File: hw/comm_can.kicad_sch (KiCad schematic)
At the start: 22 parts, among them IC601 ADM3055EBRIZ, J601 43650-0427, J602 43650-0427

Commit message: bugfix for wrong adc pin for batt current measurements
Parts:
- C602, C603, C608: Cost 0.0008 -> 0.0063; LCSC Part # C1525 -> CL05B104KB54PNC; Notes Rated for 16V. -> Rated for 50V.; P/N CL05B104KO5NNNC -> CL05B104KB54PNC
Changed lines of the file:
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@@
       (effects (font (size 1 1)) hide)
     )
-    (property "Datasheet" "https://datasheet.lcsc.com/lcsc/2304140030_Samsung-Electro-Mechanics-CL05B104KO5NNNC_C1525.pdf" (at 60.96 97.79 0)
+    (property "Datasheet" "https://datasheet.lcsc.com/lcsc/2304140030_Samsung-Electro-Mechanics-CL05B104KB54PNC_C307331.pdf" (at 60.96 97.79 0)
       (effects (font (size 1 1)) hide)
     )
@@
       (effects (font (size 1 1)) hide)
     )
-    (property "P/N" "CL05B104KO5NNNC" (at 60.96 97.79 0)
-      (effects (font (size 1 1)) hide)
-    )
-    (property "LCSC Part #" "C1525" (at 60.96 97.79 0)
-      (effects (font (size 1 1)) hide)
-    )
-    (property "Cost" "0.0008" (at 60.96 97.79 0)
-      (effects (font (size 1 1)) hide)
-    )
-    (property "Notes" "Rated for 16V." (at 60.96 97.79 0)
+    (property "P/N" "CL05B104KB54PNC" (at 60.96 97.79 0)
+      (effects (font (size 1 1)) hide)
+    )
+    (property "LCSC Part #" "CL05B104KB54PNC" (at 60.96 97.79 0)
+      (effects (font (size 1 1)) hide)
+    )
+    (property "Cost" "0.0063" (at 60.96 97.79 0)
+      (effects (font (size 1 1)) hide)
+    )
+    (property "Notes" "Rated for 50V." (at 60.96 97.79 0)
       (effects (font (size 1 1)) hide)
     )
@@
       (effects (font (size 1 1)) hide)
     )
-    (property "Datasheet" "https://datasheet.lcsc.com/lcsc/2304140030_Samsung-Electro-Mechanics-CL05B104KO5NNNC_C1525.pdf" (at 171.45 96.52 0)
+    (property "Datasheet" "https://datasheet.lcsc.com/lcsc/2304140030_Samsung-Electro-Mechanics-CL05B104KB54PNC_C307331.pdf" (at 171.45 96.52 0)
       (effects (font (size 1 1)) hide)
     )
@@
       (effects (font (size 1 1)) hide)
     )
-    (property "P/N" "CL05B104KO5NNNC" (at 171.45 96.52 0)
-      (effects (font (size 1 1)) hide)
-    )
-    (property "LCSC Part #" "C1525" (at 171.45 96.52 0)
-      (effects (font (size 1 1)) hide)
-    )
-    (property "Cost" "0.0008" (at 171.45 96.52 0)
-      (effects (font (size 1 1)) hide)
-    )
-    (property "Notes" "Rated for 16V." (at 171.45 96.52 0)
+    (property "P/N" "CL05B104KB54PNC" (at 171.45 96.52 0)
+      (effects (font (size 1 1)) hide)
+    )
+    (property "LCSC Part #" "CL05B104KB54PNC" (at 171.45 96.52 0)
+      (effects (font (size 1 1)) hide)
+    )
+    (property "Cost" "0.0063" (at 171.45 96.52 0)
+      (effects (font (size 1 1)) hide)
+    )
+    (property "Notes" "Rated for 50V." (at 171.45 96.52 0)
       (effects (font (size 1 1)) hide)
     )
@@
       (effects (font (size 1 1)) hide)
     )
-    (property "Datasheet" "https://datasheet.lcsc.com/lcsc/2304140030_Samsung-Electro-Mechanics-CL05B104KO5NNNC_C1525.pdf" (at 71.12 97.79 0)
+    (property "Datasheet" "https://datasheet.lcsc.com/lcsc/2304140030_Samsung-Electro-Mechanics-CL05B104KB54PNC_C307331.pdf" (at 71.12 97.79 0)
       (effects (font (size 1 1)) hide)
     )
@@
       (effects (font (size 1 1)) hide)
     )
-    (property "P/N" "CL05B104KO5NNNC" (at 71.12 97.79 0)
-      (effects (font (size 1 1)) hide)
-    )
-    (property "LCSC Part #" "C1525" (at 71.12 97.79 0)
-      (effects (font (size 1 1)) hide)
-    )
-    (property "Cost" "0.0008" (at 71.12 97.79 0)
-      (effects (font (size 1 1)) hide)
-    )
-    (property "Notes" "Rated for 16V." (at 71.12 97.79 0)
+    (property "P/N" "CL05B104KB54PNC" (at 71.12 97.79 0)
+      (effects (font (size 1 1)) hide)
+    )
+    (property "LCSC Part #" "CL05B104KB54PNC" (at 71.12 97.79 0)
+      (effects (font (size 1 1)) hide)
+    )
+    (property "Cost" "0.0063" (at 71.12 97.79 0)
+      (effects (font (size 1 1)) hide)
+    )
+    (property "Notes" "Rated for 50V." (at 71.12 97.79 0)
       (effects (font (size 1 1)) hide)
     )
@@
       (effects (font (size 1 1)) hide)
     )
-    (property "Datasheet" "~" (at 189.23 99.06 0)
-      (effects (font (size 1 1)) hide)
-    )
+    (property "Datasheet" "" (at 189.23 99.06 0)
+      (effects (font (size 1 1)) hide)
+    )

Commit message: init sch changes
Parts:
- removed C601, C606: 10uF, Capacitor_SMD:C_0402_1005Metric, symbol Device:C_Small
- removed C602, C603, C608: 100nF, Capacitor_SMD:C_0402_1005Metric, symbol Device:C_Small
- removed C604, C607: 10nF, Capacitor_SMD:C_0402_1005Metric, symbol Device:C_Small
- removed C605: 220nF, Capacitor_SMD:C_0402_1005Metric, symbol Device:C_Small
- removed D601: CDSOT23-T24CAN, footprints:bourns_CDSOT23_T24CAN, symbol bourns_CDSOT23_T24CAN:CDSOT23-T24CAN
- removed IC601: ADM3055EBRIZ, footprints:analog_ADM3055EBRIZ, symbol analog_ADM3055EBRIZ:ADM3055EBRIZ
- removed J601, J602: 43650-0427, footprints:molex_microfit_43650_0427, symbol molex_microfit_43650_0427:43650-0427
- removed JP601: Termination Resistors, Connector_PinHeader_2.54mm:PinHeader_1x02_P2.54mm_Vertical, symbol Jumper:Jumper_2_Open
- removed L601, L602: 1.8k, Inductor_SMD:L_0402_1005Metric, symbol Device:FerriteBead_Small
- removed R601: 0, Resistor_SMD:R_0402_1005Metric, symbol Device:R
- removed R602, R603: 60.4, Resistor_SMD:R_0402_1005Metric, symbol Device:R
- removed TP601: CAN RX TP, TestPoint:TestPoint_Pad_1.0x1.0mm, symbol Connector:TestPoint
- removed TP602: CAN TX TP, TestPoint:TestPoint_Pad_1.0x1.0mm, symbol Connector:TestPoint
- removed TP603: CAN L TP, TestPoint:TestPoint_Pad_1.0x1.0mm, symbol Connector:TestPoint
- removed TP604: CAN H TP, TestPoint:TestPoint_Pad_1.0x1.0mm, symbol Connector:TestPoint
- added C24, C25: 100nF, symbol Device:C_Small
- added D5: CDSOT23-T24CAN, footprints:bourns_CDSOT23_T24CAN, symbol bourns_CDSOT23_T24CAN:CDSOT23-T24CAN
- added J2, J3: 43650-0427, footprints:molex_microfit_43650_0427, symbol molex_microfit_43650_0427:43650-0427
- added JP1: Termination Resistors, Connector_PinHeader_2.54mm:PinHeader_1x02_P2.54mm_Vertical, symbol Jumper:Jumper_2_Open
- added R12: 120, symbol Device:R_Small
- added TP10: CAN_{TX}, symbol Connector:TestPoint
- added TP11: CAN_{VCC}, symbol Connector:TestPoint
- added TP12: CAN_{H}, symbol Connector:TestPoint
- added TP13: CAN_{L}, symbol Connector:TestPoint
- added TP14: CAN_{GND}, symbol Connector:TestPoint
- added TP9: CAN_{RX}, symbol Connector:TestPoint
- added U7: ISO1044BD, Package_SO:SOIC-8_3.9x4.9mm_P1.27mm, symbol Interface_CAN_LIN:ISO1044BD
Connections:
- net +3V3: now also C24.1, U7.1 (VCC1)
- net CAN_RX: now also TP9.1, U7.3 (RXD)
- net CAN_TX: now also TP10.1, U7.2 (TXD)
- net GND: now also C24.2, U7.4 (GND1)
- new net: JP1.2 (B), R12.1
- new net CAN_{GND}: C25.2, D5.3 (K3), J2.2, J3.2, TP14.1, U7.7 (GND2)
- new net CAN_{H}: D5.1 (K1), J2.3, J3.3, R12.2, TP12.1, U7.6 (CANH)
- new net CAN_{L}: D5.2 (K2), J2.4, J3.4, JP1.1 (A), TP13.1, U7.5 (CANL)
- new net CAN_{VCC}: C25.1, J2.1, J3.1, TP11.1, U7.8 (VCC2)
- no-connect marks 4 -> 0
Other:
- note removed: "Must be close to V_ISO_In"
- note removed: "Must be close to V_ISO_Out"

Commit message: v0.3.0rc (v1.0.0rc) sch complete
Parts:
- removed C24: 100nF, symbol Device:C_Small
- removed J3: 43650-0427, footprints:molex_microfit_43650_0427, symbol molex_microfit_43650_0427:43650-0427
- removed TP10: CAN_{TX}, symbol Connector:TestPoint
- removed TP11: CAN_{VCC}, symbol Connector:TestPoint
- removed TP12: CAN_{H}, symbol Connector:TestPoint
- removed TP13: CAN_{L}, symbol Connector:TestPoint
- removed TP14: CAN_{GND}, symbol Connector:TestPoint
- removed TP9: CAN_{RX}, symbol Connector:TestPoint
- added C601: 4.7u, Resistor_SMD:R_0402_1005Metric, symbol Device:C_Small
- added C603: 100n, Resistor_SMD:R_0402_1005Metric, symbol Device:C_Small
- added C604, C605: 1u, Resistor_SMD:R_0402_1005Metric, symbol Device:C_Small
- added D601, D602: GRN, LED_SMD:LED_0402_1005Metric, symbol Device:LED_Small
- added J602: CAN Header, footprints:molex_microfit_43650_0427, symbol molex_microfit_43650_0427:43650-0427
- added R601: 330, Resistor_SMD:R_0402_1005Metric, symbol Device:R_Small
- added R603: 1k, Resistor_SMD:R_0402_1005Metric, symbol Device:R_Small
- added SB601, SB602: Jumper, Jumper:SolderJumper-2_P1.3mm_Open_TrianglePad1.0x1.5mm, symbol Jumper:SolderJumper_2_Bridged
- added TP601: VBUS_CAN, TestPoint:TestPoint_Keystone_5000-5004_Miniature, symbol Connector:TestPoint
- added TP602: GND, TestPoint:TestPoint_Keystone_5000-5004_Miniature, symbol Connector:TestPoint
- added TP603: CAN_TX, TestPoint:TestPoint_Keystone_5000-5004_Miniature, symbol Connector:TestPoint
- added TP604: CAN_RX, TestPoint:TestPoint_Keystone_5000-5004_Miniature, symbol Connector:TestPoint
- added TP605: VBUS_CAN_ISO, TestPoint:TestPoint_Keystone_5000-5004_Miniature, symbol Connector:TestPoint
- added TP606: GNDPWR, TestPoint:TestPoint_Keystone_5000-5004_Miniature, symbol Connector:TestPoint
- added TP607: CAN_H, TestPoint:TestPoint_Keystone_5000-5004_Miniature, symbol Connector:TestPoint
- added TP608: CAN_L, TestPoint:TestPoint_Keystone_5000-5004_Miniature, symbol Connector:TestPoint
- C602: renamed from C25; value 100nF -> 100n; footprint (none) -> Resistor_SMD:R_0402_1005Metric; Cost (none) -> 0.0046; Distributor (none) -> LCSC; LCSC Part # (none) -> C307331; Manufacturer (none) -> Samsung Electromechanics; Notes (none) -> Recommended value.; P/N (none) -> CL05B104KB54PNC
- D603: renamed from D5; Cost 0.1982 -> 0.36; Distributor JLCPCB -> Mouser; LCSC Part # C350941 -> (none)
- J601: renamed from J2; value 43650-0427 -> CAN Header; Cost 1.41 -> 1.40
- JP601: renamed from JP1; value Termination Resistors -> Jumper_2_Bridged; Cost (none) -> 0.1; Distributor (none) -> Mouser; Manufacturer (none) -> Samtec; Notes (none) -> Requires jumper (PRT-09044, 0.38); P/N (none) -> TSW-102-07-T-S
- R602: renamed from R12; footprint (none) -> Resistor_SMD:R_0402_1005Metric; Cost (none) -> 0.0005; Distributor (none) -> LCSC; LCSC Part # (none) -> C25079; Manufacturer (none) -> Uniroyal; P/N (none) -> 0402WGF1200TCE
- U601: renamed from U7; value ISO1044BD -> ISO1044; Cost (none) -> 2.343; Distributor (none) -> Texas Instruments; Manufacturer (none) -> Texas Instruments; Notes (none) -> 5Mbps, +-58V; P/N (none) -> ISO1044BDR
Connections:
- net +3V3: now also SB601.1 (A); no longer U601.1 (VCC1)
- net CAN_RX: now also TP604.1
- net CAN_TX: now also TP603.1
- net GND: now also C601.2, C603.2, C604.2, D601.1 (K), TP602.1
- net CAN_{GND} renamed GNDPWR
- net GNDPWR: now also C605.2, D602.1 (K), J602.2, TP606.1
- net CAN_{H} renamed CAN_H
- net CAN_H: now also J602.3, TP607.1
- net CAN_{L} renamed CAN_L
- net CAN_L: now also J602.4, TP608.1
- net CAN_{VCC} renamed VBUS_CAN_ISO
- net VBUS_CAN_ISO: now also C605.1, J602.1, R603.1, SB602.2 (B), TP605.1
- new net: D601.2 (A), R601.2
- new net: D602.2 (A), R603.2
- new net +5VP: SB602.1 (A)
- new net VBUS_CAN: C601.1, C603.1, C604.1, R601.1, SB601.2 (B), TP601.1, U601.1 (VCC1)
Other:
- note removed: "CAN Bus Protection"
- moved on the sheet: C602, D603, J601, JP601, R602, U601

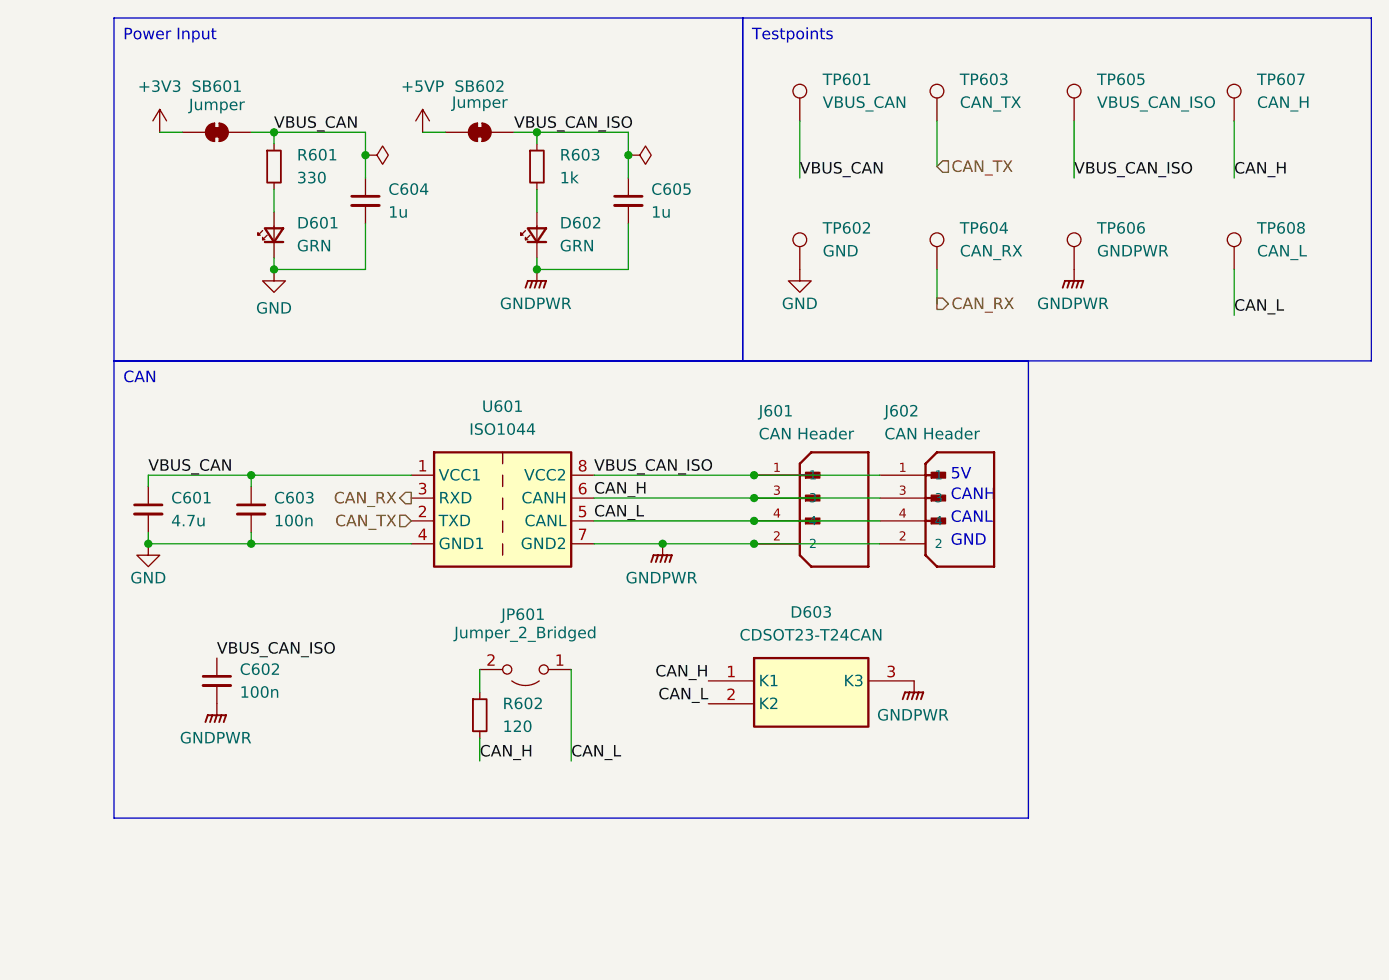
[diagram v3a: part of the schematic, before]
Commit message: HW sch changes, further layout progression
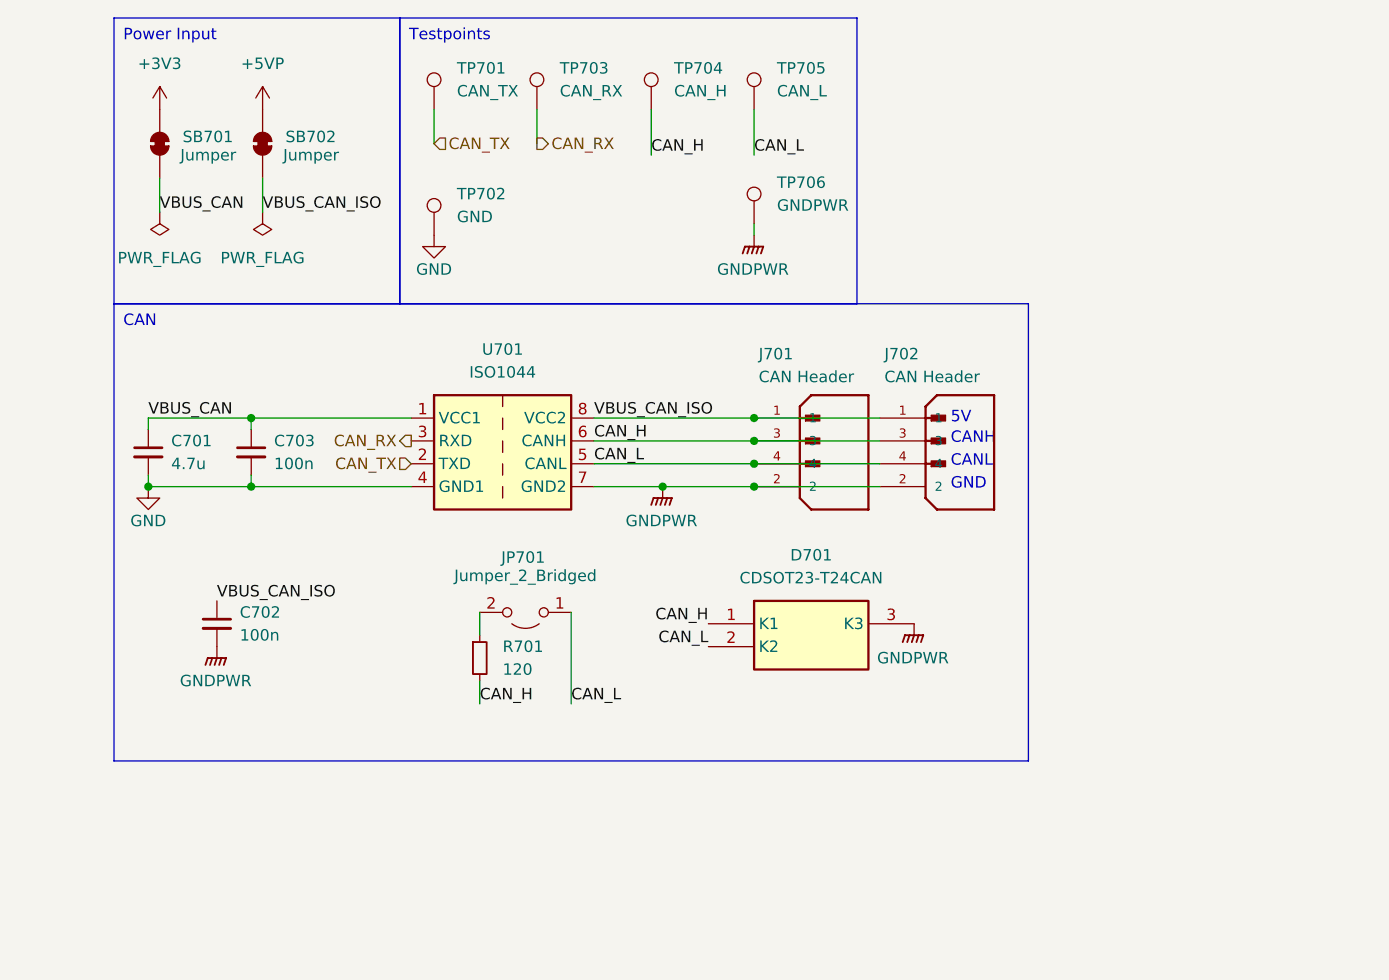
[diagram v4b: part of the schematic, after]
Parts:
- removed C604, C605: 1u, Resistor_SMD:R_0402_1005Metric, symbol Device:C_Small
- removed D601, D602: GRN, LED_SMD:LED_0402_1005Metric, symbol Device:LED_Small
- removed R601: 330, Resistor_SMD:R_0402_1005Metric, symbol Device:R_Small
- removed R603: 1k, Resistor_SMD:R_0402_1005Metric, symbol Device:R_Small
- removed SB602: Jumper, Jumper:SolderJumper-2_P1.3mm_Open_TrianglePad1.0x1.5mm, symbol Jumper:SolderJumper_2_Bridged
- removed TP601: VBUS_CAN, TestPoint:TestPoint_Keystone_5000-5004_Miniature, symbol Connector:TestPoint
- removed TP605: VBUS_CAN_ISO, TestPoint:TestPoint_Keystone_5000-5004_Miniature, symbol Connector:TestPoint
- added SB702: Jumper, Jumper:SolderJumper-2_P1.3mm_Open_TrianglePad1.0x1.5mm, symbol Jumper:SolderJumper_2_Bridged
- TP701: renamed from TP603; footprint TestPoint:TestPoint_Keystone_5000-5004_Miniature -> TestPoint:TestPoint_Pad_D1.5mm; Cost 0.38 -> (none); Distributor Mouser -> (none); Manufacturer Keystone Electronics -> (none); Notes White (Digital Signal) -> (none); P/N 5002 -> (none)
- TP702: renamed from TP602; footprint TestPoint:TestPoint_Keystone_5000-5004_Miniature -> TestPoint:TestPoint_Pad_D1.5mm; Cost 0.37 -> (none); Distributor Mouser -> (none); Manufacturer Keystone Electronics -> (none); Notes Black (Logic Ground) -> (none); P/N 5001 -> (none)
- TP703: renamed from TP604; footprint TestPoint:TestPoint_Keystone_5000-5004_Miniature -> TestPoint:TestPoint_Pad_D1.5mm; Cost 0.38 -> (none); Distributor Mouser -> (none); Manufacturer Keystone Electronics -> (none); Notes White (Digital Signal) -> (none); P/N 5002 -> (none)
- TP704: renamed from TP607; footprint TestPoint:TestPoint_Keystone_5000-5004_Miniature -> TestPoint:TestPoint_Pad_D1.5mm; Cost 0.38 -> (none); Distributor Mouser -> (none); Manufacturer Keystone Electronics -> (none); Notes White (Digital Signal) -> (none); P/N 5002 -> (none)
- TP705: renamed from TP608; footprint TestPoint:TestPoint_Keystone_5000-5004_Miniature -> TestPoint:TestPoint_Pad_D1.5mm; Cost 0.38 -> (none); Distributor Mouser -> (none); Manufacturer Keystone Electronics -> (none); Notes White (Digital Signal) -> (none); P/N 5002 -> (none)
- TP706: renamed from TP606; footprint TestPoint:TestPoint_Keystone_5000-5004_Miniature -> TestPoint:TestPoint_Pad_D1.5mm; Cost 0.37 -> (none); Distributor Mouser -> (none); Manufacturer Keystone Electronics -> (none); Notes Brown (Power Path Ground) -> (none); P/N 5115 -> (none)
- renumbered C601 to C701, C602 to C702, C603 to C703, D603 to D701, J601 to J701, J602 to J702, JP601 to JP701, R602 to R701, SB601 to SB701, U601 to U701
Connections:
- net +5VP: now also SB702.1 (A)
- net VBUS_CAN_ISO: now also SB702.2 (B)
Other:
- moved on the sheet: C701, C702, C703, D701, J701, J702, JP701, R701, SB701, TP701, TP702, TP703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
